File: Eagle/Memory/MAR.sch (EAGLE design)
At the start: 1 part, among them J1 55959-1430

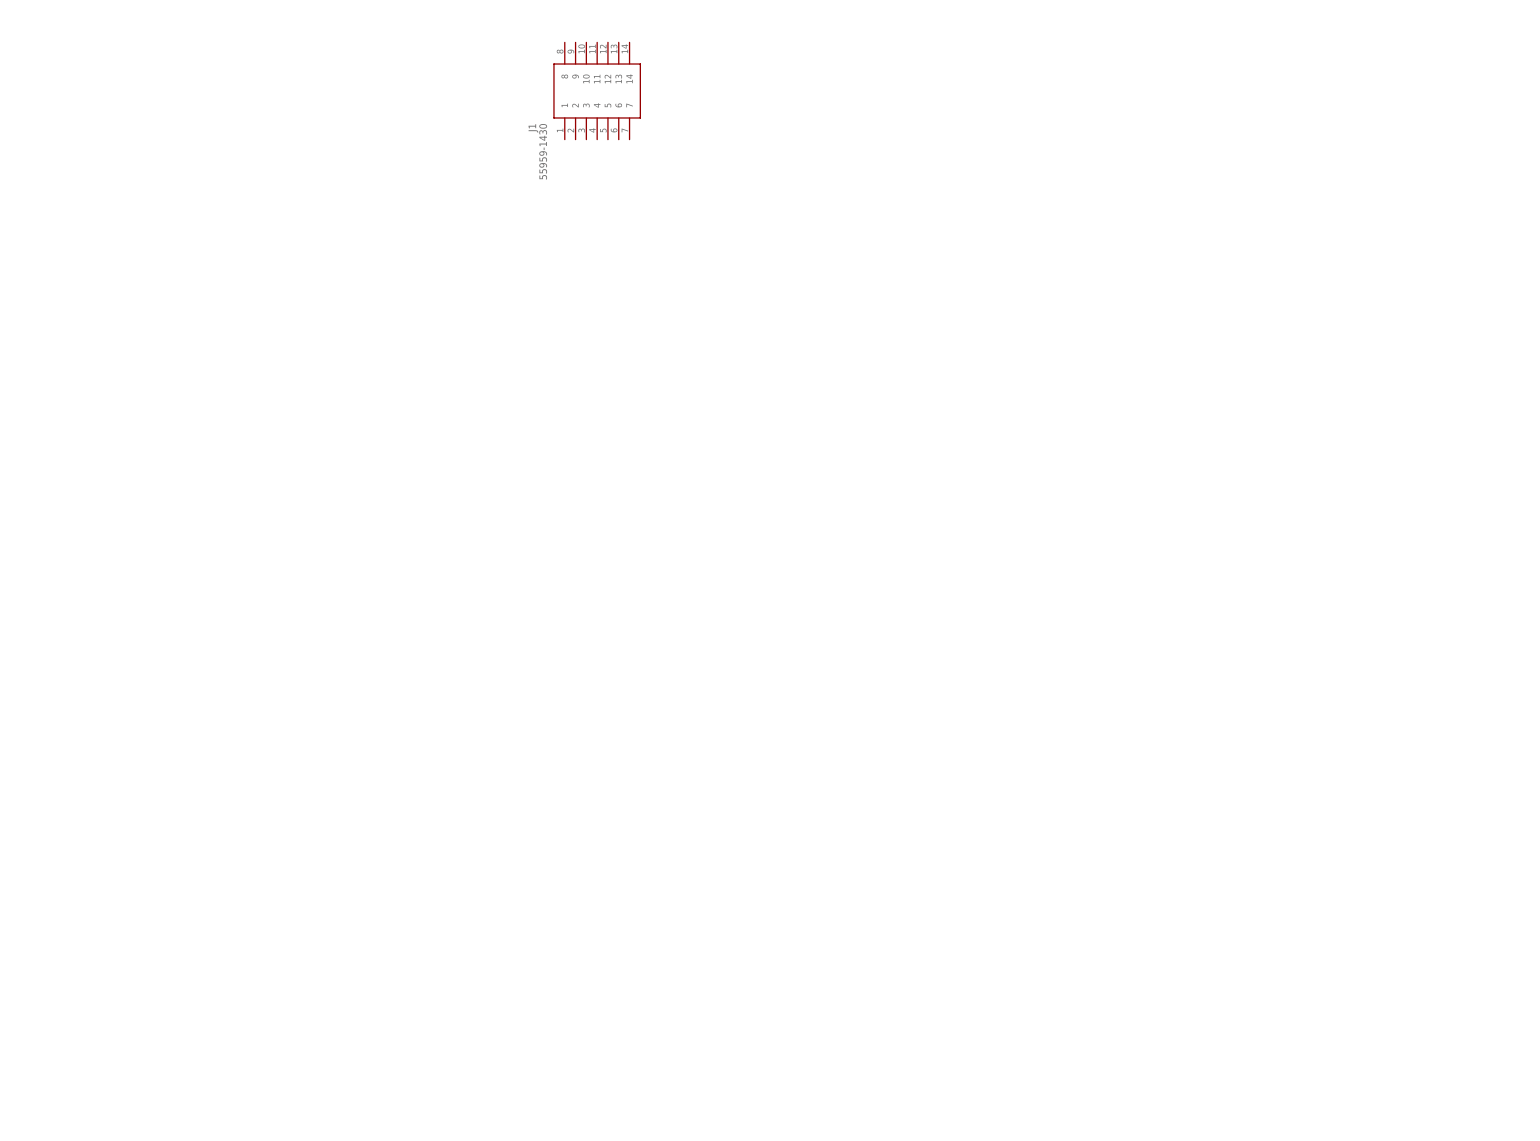
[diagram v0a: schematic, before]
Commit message: fixed skipcond logic in logisim and added more registers to MARIE
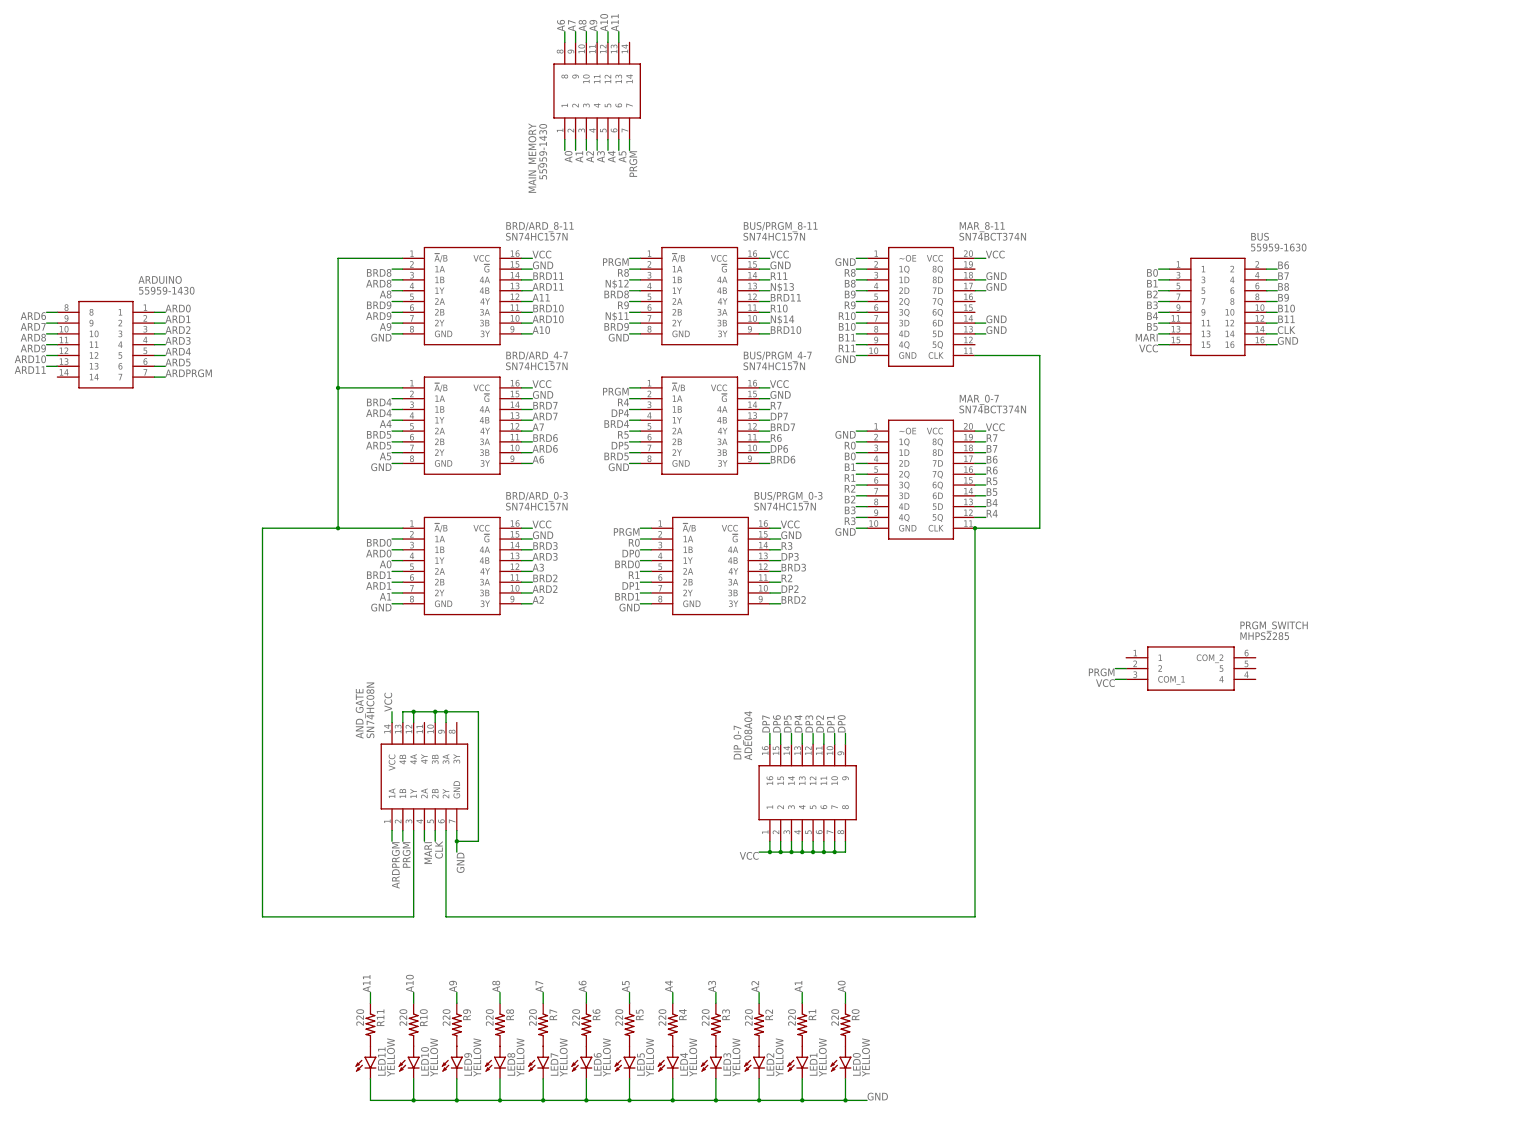
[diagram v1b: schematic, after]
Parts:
- added AND_GATE: SN74HC08N, SamacSys_Parts:SN74HC08N
- added ARDUINO: 55959-1430, SamacSys_Parts:55959-1430
- added BRD/ARD_0-3, BRD/ARD_4-7, BRD/ARD_8-11, BUS/PRGM_0-3, BUS/PRGM_4-7, BUS/PRGM_8-11: SN74HC157N, SamacSys_Parts:SN74HC157N
- added BUS: 55959-1630, SamacSys_Parts:55959-1630
- added DIP_0-7: ADE08A04, SamacSys_Parts:ADE08A04
- added LED0, LED1, LED10, LED11, LED2, LED3, LED4, LED5, LED6, LED7, LED8, LED9: YELLOW, led:LED3MM
- added MAR_0-7, MAR_8-11: SN74BCT374N, SamacSys_Parts:SN74BCT374N
- added PRGM_SWITCH: MHPS2285, SamacSys_Parts:MHPS2285
- added R0, R1, R10, R11, R2, R3, R4, R5, R6, R7, R8, R9: 220, rcl:R-US_0204/7
- renumbered J1 to MAIN_MEMORY
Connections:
- new net A0: BRD/ARD_0-3.1Y, MAIN_MEMORY.1, R0.1
- new net A1: BRD/ARD_0-3.2Y, MAIN_MEMORY.2, R1.1
- new net A10: BRD/ARD_8-11.3Y, MAIN_MEMORY.12, R10.1
- new net A11: BRD/ARD_8-11.4Y, MAIN_MEMORY.13, R11.1
- new net A2: BRD/ARD_0-3.3Y, MAIN_MEMORY.3, R2.1
- new net A3: BRD/ARD_0-3.4Y, MAIN_MEMORY.4, R3.1
- new net A4: BRD/ARD_4-7.1Y, MAIN_MEMORY.5, R4.1
- new net A5: BRD/ARD_4-7.2Y, MAIN_MEMORY.6, R5.1
- new net A6: BRD/ARD_4-7.3Y, MAIN_MEMORY.8, R6.1
- new net A7: BRD/ARD_4-7.4Y, MAIN_MEMORY.9, R7.1
- new net A8: BRD/ARD_8-11.1Y, MAIN_MEMORY.10, R8.1
- new net A9: BRD/ARD_8-11.2Y, MAIN_MEMORY.11, R9.1
- new net ARD0: ARDUINO.1, BRD/ARD_0-3.1B
- new net ARD1: ARDUINO.2, BRD/ARD_0-3.2B
- new net ARD10: ARDUINO.12, BRD/ARD_8-11.3B
- new net ARD11: ARDUINO.13, BRD/ARD_8-11.4B
- new net ARD2: ARDUINO.3, BRD/ARD_0-3.3B
- new net ARD3: ARDUINO.4, BRD/ARD_0-3.4B
- new net ARD4: ARDUINO.5, BRD/ARD_4-7.1B
- new net ARD5: ARDUINO.6, BRD/ARD_4-7.2B
- new net ARD6: ARDUINO.8, BRD/ARD_4-7.3B
- new net ARD7: ARDUINO.9, BRD/ARD_4-7.4B
- new net ARD8: ARDUINO.10, BRD/ARD_8-11.1B
- new net ARD9: ARDUINO.11, BRD/ARD_8-11.2B
- new net ARDPRGM: AND_GATE.1A, ARDUINO.7
- new net B0: BUS.1, MAR_0-7.1D
- new net B1: BUS.3, MAR_0-7.2D
- new net B10: BUS.10, MAR_8-11.3D
- new net B11: BUS.12, MAR_8-11.4D
- new net B2: BUS.5, MAR_0-7.3D
- new net B3: BUS.7, MAR_0-7.4D
- new net B4: BUS.9, MAR_0-7.5D
- new net B5: BUS.11, MAR_0-7.6D
- new net B6: BUS.2, MAR_0-7.7D
- new net B7: BUS.4, MAR_0-7.8D
- new net B8: BUS.6, MAR_8-11.1D
- new net B9: BUS.8, MAR_8-11.2D
- new net BRD0: BRD/ARD_0-3.1A, BUS/PRGM_0-3.1Y
- new net BRD1: BRD/ARD_0-3.2A, BUS/PRGM_0-3.2Y
- new net BRD10: BRD/ARD_8-11.3A, BUS/PRGM_8-11.3Y
- new net BRD11: BRD/ARD_8-11.4A, BUS/PRGM_8-11.4Y
- new net BRD2: BRD/ARD_0-3.3A, BUS/PRGM_0-3.3Y
- new net BRD3: BRD/ARD_0-3.4A, BUS/PRGM_0-3.4Y
- new net BRD4: BRD/ARD_4-7.1A, BUS/PRGM_4-7.1Y
- new net BRD5: BRD/ARD_4-7.2A, BUS/PRGM_4-7.2Y
- new net BRD6: BRD/ARD_4-7.3A, BUS/PRGM_4-7.3Y
- new net BRD7: BRD/ARD_4-7.4A, BUS/PRGM_4-7.4Y
- new net BRD8: BRD/ARD_8-11.1A, BUS/PRGM_8-11.1Y
- new net BRD9: BRD/ARD_8-11.2A, BUS/PRGM_8-11.2Y
- new net CLK: AND_GATE.2B, BUS.14
- new net DP0: BUS/PRGM_0-3.1B, DIP_0-7.9
- new net DP1: BUS/PRGM_0-3.2B, DIP_0-7.10
- new net DP2: BUS/PRGM_0-3.3B, DIP_0-7.11
- new net DP3: BUS/PRGM_0-3.4B, DIP_0-7.12
- new net DP4: BUS/PRGM_4-7.1B, DIP_0-7.13
- new net DP5: BUS/PRGM_4-7.2B, DIP_0-7.14
- new net DP6: BUS/PRGM_4-7.3B, DIP_0-7.15
- new net DP7: BUS/PRGM_4-7.4B, DIP_0-7.16
- new net GND: AND_GATE.3A, AND_GATE.3B, AND_GATE.4A, AND_GATE.4B, AND_GATE.GND, BRD/ARD_0-3.!G, BRD/ARD_0-3.GND, BRD/ARD_4-7.!G, BRD/ARD_4-7.GND, BRD/ARD_8-11.!G, BRD/ARD_8-11.GND, BUS.16, BUS/PRGM_0-3.!G, BUS/PRGM_0-3.GND, BUS/PRGM_4-7.!G, BUS/PRGM_4-7.GND, BUS/PRGM_8-11.!G, BUS/PRGM_8-11.GND, LED0.C, LED1.C, LED10.C, LED11.C, LED2.C, LED3.C, LED4.C, LED5.C, LED6.C, LED7.C, LED8.C, LED9.C, MAR_0-7.GND, MAR_0-7.~OE, MAR_8-11.5D, MAR_8-11.6D, MAR_8-11.7D, MAR_8-11.8D, MAR_8-11.GND, MAR_8-11.~OE
- new net MARI: AND_GATE.2A, BUS.13
- new net N$1: AND_GATE.1Y, BRD/ARD_0-3.!A!/B, BRD/ARD_4-7.!A!/B, BRD/ARD_8-11.!A!/B
- new net N$10: LED8.A, R8.2
- new net N$11: BUS/PRGM_8-11.2B
- new net N$12: BUS/PRGM_8-11.1B
- new net N$13: BUS/PRGM_8-11.4B
- new net N$14: BUS/PRGM_8-11.3B
- new net N$15: LED9.A, R9.2
- new net N$16: LED10.A, R10.2
- new net N$17: LED11.A, R11.2
- new net N$2: AND_GATE.2Y, MAR_0-7.CLK, MAR_8-11.CLK
- new net N$22: LED0.A, R0.2
- new net N$3: LED1.A, R1.2
- new net N$4: LED2.A, R2.2
- new net N$5: LED3.A, R3.2
- new net N$6: LED4.A, R4.2
- new net N$7: LED5.A, R5.2
- new net N$8: LED6.A, R6.2
- new net N$9: LED7.A, R7.2
- new net PRGM: AND_GATE.1B, BUS/PRGM_0-3.!A!/B, BUS/PRGM_4-7.!A!/B, BUS/PRGM_8-11.!A!/B, MAIN_MEMORY.7, PRGM_SWITCH.2
- new net R0: BUS/PRGM_0-3.1A, MAR_0-7.1Q
- new net R1: BUS/PRGM_0-3.2A, MAR_0-7.2Q
- new net R10: BUS/PRGM_8-11.3A, MAR_8-11.3Q
- new net R11: BUS/PRGM_8-11.4A, MAR_8-11.4Q
- new net R2: BUS/PRGM_0-3.3A, MAR_0-7.3Q
- new net R3: BUS/PRGM_0-3.4A, MAR_0-7.4Q
- new net R4: BUS/PRGM_4-7.1A, MAR_0-7.5Q
- new net R5: BUS/PRGM_4-7.2A, MAR_0-7.6Q
- new net R6: BUS/PRGM_4-7.3A, MAR_0-7.7Q
- new net R7: BUS/PRGM_4-7.4A, MAR_0-7.8Q
- new net R8: BUS/PRGM_8-11.1A, MAR_8-11.1Q
- new net R9: BUS/PRGM_8-11.2A, MAR_8-11.2Q
- new net VCC: AND_GATE.VCC, BRD/ARD_0-3.VCC, BRD/ARD_4-7.VCC, BRD/ARD_8-11.VCC, BUS.15, BUS/PRGM_0-3.VCC, BUS/PRGM_4-7.VCC, BUS/PRGM_8-11.VCC, DIP_0-7.1, DIP_0-7.2, DIP_0-7.3, DIP_0-7.4, DIP_0-7.5, DIP_0-7.6, DIP_0-7.7, DIP_0-7.8, MAR_0-7.VCC, MAR_8-11.VCC, PRGM_SWITCH.COM_1

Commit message: Worked on IR
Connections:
- net B10: now also BUS.6; no longer BUS.10
- net B11: now also BUS.8; no longer BUS.12
- net B6: now also BUS.13; no longer BUS.2
- net B7: now also BUS.15; no longer BUS.4
- net B8: now also BUS.2; no longer BUS.6
- net B9: now also BUS.4; no longer BUS.8
- net MARI: now also BUS.10; no longer BUS.13
- net VCC: now also BUS.12; no longer BUS.15
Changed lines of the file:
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@@
 <net name="B6" class="0">
+<segment>
+<pinref part="MAR_0-7" gate="G$1" pin="7D"/>
+<wire x1="147.32" y1="-10.16" x2="149.86" y2="-10.16" width="0.1524" layer="91"/>
+<label x="149.86" y="-10.16" size="1.778" layer="95"/>
+</segment>
+<segment>
+<pinref part="BUS" gate="G$1" pin="13"/>
+<wire x1="193.04" y1="20.32" x2="190.5" y2="20.32" width="0.1524" layer="91"/>
+<label x="190.5" y="20.32" size="1.778" layer="95" rot="R180"/>
+</segment>
+</net>
+<net name="B7" class="0">
+<segment>
+<pinref part="MAR_0-7" gate="G$1" pin="8D"/>
+<wire x1="147.32" y1="-7.62" x2="149.86" y2="-7.62" width="0.1524" layer="91"/>
+<label x="149.86" y="-7.62" size="1.778" layer="95"/>
+</segment>
+<segment>
+<pinref part="BUS" gate="G$1" pin="15"/>
+<wire x1="193.04" y1="17.78" x2="190.5" y2="17.78" width="0.1524" layer="91"/>
+<label x="190.5" y="17.78" size="1.778" layer="95" rot="R180"/>
+</segment>
+</net>
+<net name="B8" class="0">
+<segment>
+<pinref part="MAR_8-11" gate="G$1" pin="1D"/>
+<wire x1="121.92" y1="33.02" x2="119.38" y2="33.02" width="0.1524" layer="91"/>
+<label x="119.38" y="33.02" size="1.778" layer="95" rot="R180"/>
+</segment>
 <segment>
 <pinref part="BUS" gate="G$1" pin="2"/>
@@
 <label x="218.44" y="35.56" size="1.778" layer="95"/>
 </segment>
+</net>
+<net name="B9" class="0">
 <segment>
-<pinref part="MAR_0-7" gate="G$1" pin="7D"/>
-<wire x1="147.32" y1="-10.16" x2="149.86" y2="-10.16" width="0.1524" layer="91"/>
-<label x="149.86" y="-10.16" size="1.778" layer="95"/>
+<pinref part="MAR_8-11" gate="G$1" pin="2D"/>
+<wire x1="121.92" y1="30.48" x2="119.38" y2="30.48" width="0.1524" layer="91"/>
+<label x="119.38" y="30.48" size="1.778" layer="95" rot="R180"/>
 </segment>
-</net>
-<net name="B7" class="0">
 <segment>
 <pinref part="BUS" gate="G$1" pin="4"/>
@@
 <label x="218.44" y="33.02" size="1.778" layer="95"/>
 </segment>
+</net>
+<net name="B10" class="0">
 <segment>
-<pinref part="MAR_0-7" gate="G$1" pin="8D"/>
-<wire x1="147.32" y1="-7.62" x2="149.86" y2="-7.62" width="0.1524" layer="91"/>
-<label x="149.86" y="-7.62" size="1.778" layer="95"/>
+<pinref part="MAR_8-11" gate="G$1" pin="3D"/>
+<wire x1="121.92" y1="22.86" x2="119.38" y2="22.86" width="0.1524" layer="91"/>
+<label x="119.38" y="22.86" size="1.778" layer="95" rot="R180"/>
 </segment>
-</net>
-<net name="B8" class="0">
 <segment>
 <pinref part="BUS" gate="G$1" pin="6"/>
@@
 <label x="218.44" y="30.48" size="1.778" layer="95"/>
 </segment>
+</net>
+<net name="B11" class="0">
 <segment>
-<pinref part="MAR_8-11" gate="G$1" pin="1D"/>
-<wire x1="121.92" y1="33.02" x2="119.38" y2="33.02" width="0.1524" layer="91"/>
-<label x="119.38" y="33.02" size="1.778" layer="95" rot="R180"/>
+<pinref part="MAR_8-11" gate="G$1" pin="4D"/>
+<wire x1="121.92" y1="20.32" x2="119.38" y2="20.32" width="0.1524" layer="91"/>
+<label x="119.38" y="20.32" size="1.778" layer="95" rot="R180"/>
 </segment>
-</net>
-<net name="B9" class="0">
 <segment>
 <pinref part="BUS" gate="G$1" pin="8"/>
 <wire x1="215.9" y1="27.94" x2="218.44" y2="27.94" width="0.1524" layer="91"/>
 <label x="218.44" y="27.94" size="1.778" layer="95"/>
-</segment>
-<segment>
-<pinref part="MAR_8-11" gate="G$1" pin="2D"/>
-<wire x1="121.92" y1="30.48" x2="119.38" y2="30.48" width="0.1524" layer="91"/>
-<label x="119.38" y="30.48" size="1.778" layer="95" rot="R180"/>
-</segment>
-</net>
-<net name="B10" class="0">
-<segment>
-<pinref part="BUS" gate="G$1" pin="10"/>
-<wire x1="215.9" y1="25.4" x2="218.44" y2="25.4" width="0.1524" layer="91"/>
-<label x="218.44" y="25.4" size="1.778" layer="95"/>
-</segment>
-<segment>
-<pinref part="MAR_8-11" gate="G$1" pin="3D"/>
-<wire x1="121.92" y1="22.86" x2="119.38" y2="22.86" width="0.1524" layer="91"/>
-<label x="119.38" y="22.86" size="1.778" layer="95" rot="R180"/>
-</segment>
-</net>
-<net name="B11" class="0">
-<segment>
-<pinref part="BUS" gate="G$1" pin="12"/>
-<wire x1="215.9" y1="22.86" x2="218.44" y2="22.86" width="0.1524" layer="91"/>
-<label x="218.44" y="22.86" size="1.778" layer="95"/>
-</segment>
-<segment>
-<pinref part="MAR_8-11" gate="G$1" pin="4D"/>
-<wire x1="121.92" y1="20.32" x2="119.38" y2="20.32" width="0.1524" layer="91"/>
-<label x="119.38" y="20.32" size="1.778" layer="95" rot="R180"/>
 </segment>
 </net>
@@
 <net name="MARI" class="0">
 <segment>
-<pinref part="BUS" gate="G$1" pin="13"/>
-<wire x1="193.04" y1="20.32" x2="190.5" y2="20.32" width="0.1524" layer="91"/>
-<label x="190.5" y="20.32" size="1.778" layer="95" rot="R180"/>
-</segment>
-<segment>
 <pinref part="AND_GATE" gate="G$1" pin="2A"/>
 <wire x1="17.78" y1="-96.52" x2="17.78" y2="-99.06" width="0.1524" layer="91"/>
 <label x="17.78" y="-99.06" size="1.778" layer="95" rot="R270"/>
 </segment>
+<segment>
+<pinref part="BUS" gate="G$1" pin="10"/>
+<wire x1="215.9" y1="25.4" x2="218.44" y2="25.4" width="0.1524" layer="91"/>
+<label x="218.44" y="25.4" size="1.778" layer="95"/>
+</segment>
 </net>
 <net name="VCC" class="0">
-<segment>
-<pinref part="BUS" gate="G$1" pin="15"/>
-<wire x1="193.04" y1="17.78" x2="190.5" y2="17.78" width="0.1524" layer="91"/>
-<label x="190.5" y="17.78" size="1.778" layer="95" rot="R180"/>
-</segment>
 <segment>
 <pinref part="MAR_8-11" gate="G$1" pin="VCC"/>
@@
 <label x="180.34" y="-60.96" size="1.778" layer="95" rot="R180"/>
 </segment>
+<segment>
+<pinref part="BUS" gate="G$1" pin="12"/>
+<wire x1="215.9" y1="22.86" x2="218.44" y2="22.86" width="0.1524" layer="91"/>
+<label x="218.44" y="22.86" size="1.778" layer="95"/>
+</segment>
 </net>
